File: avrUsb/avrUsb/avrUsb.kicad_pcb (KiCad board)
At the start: 4 copper layers, 53 x 59 mm, 15 parts, among them J1 Screw_Terminal_01x07, J2 Screw_Terminal_01x10, J3 Screw_Terminal_01x10, U1 ATmega8U2-AU, X1 USBFCI_10103594, Y1 8 Mhz

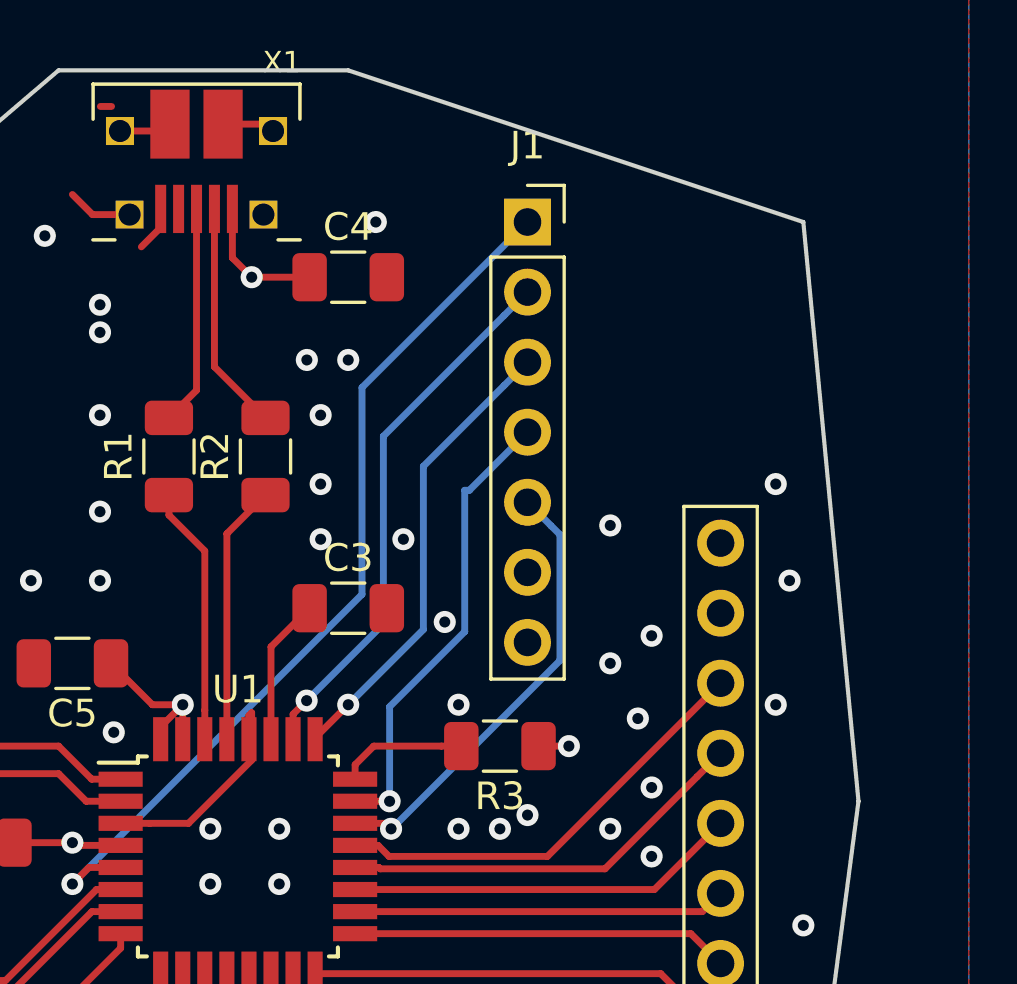
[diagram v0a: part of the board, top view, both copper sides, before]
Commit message: updated usb polarity + reset header
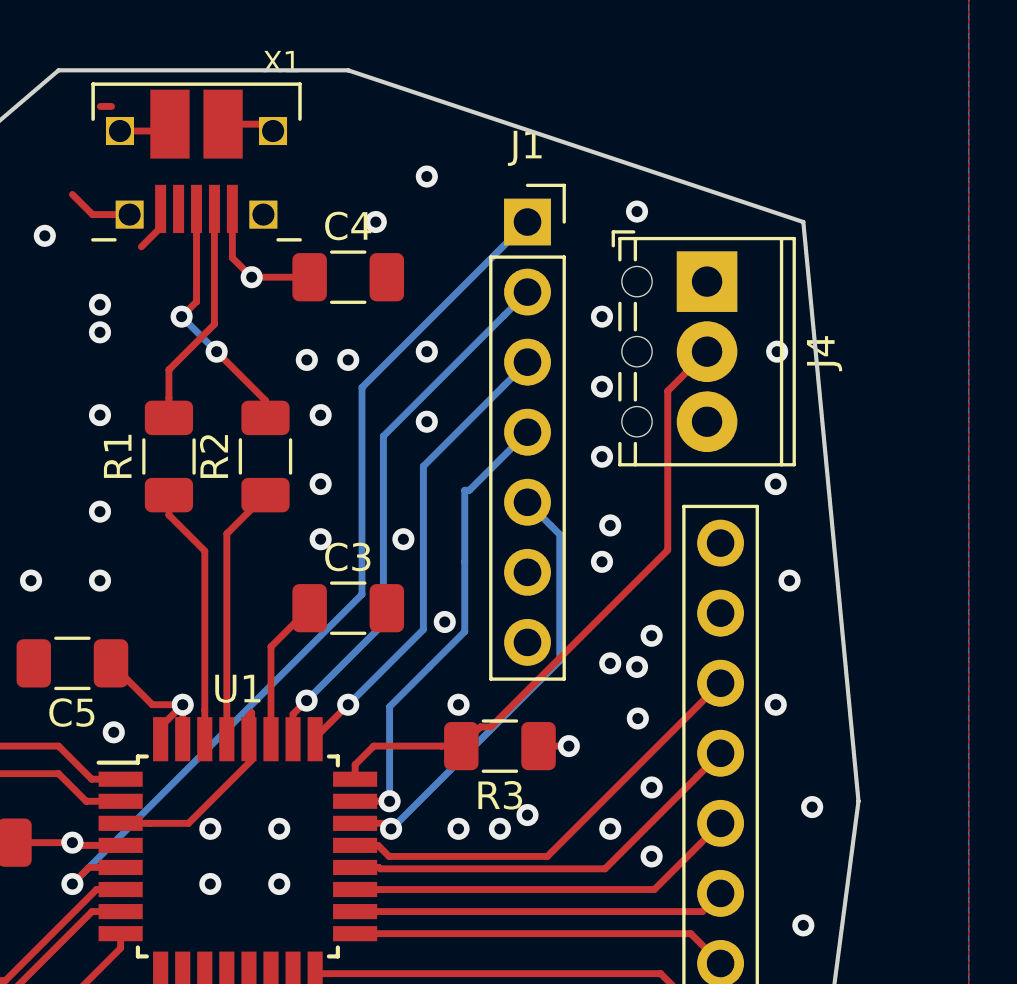
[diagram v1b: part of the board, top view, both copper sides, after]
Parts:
- added J4: Screw_Terminal_01x03, TerminalBlock_Phoenix:TerminalBlock_Phoenix_MPT-0,5-3-2.54_1x03_P2.54mm_Horizontal, F.Cu at (207.0, 73.7)
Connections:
- X1 pad D+: Net-(R1-Pad2) -> Net-(R2-Pad2)
- X1 pad D-: Net-(R2-Pad2) -> Net-(R1-Pad2)
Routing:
- net Net-(J4-Pad2): track 4.65 -> 22.9 mm
- net Net-(R2-Pad2): track 8.34 -> 9.06 mm, vias 0 -> 2
- net GND: track 16.3 -> 16.7 mm, vias 78 -> 89

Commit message: QFN
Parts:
- U1: value ATmega8U2-AU -> ATmega32U2-MU
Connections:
- U1 pad 10: Net-(J3-Pad5) -> Net-(J1-Pad2)
- U1 pad 11: Net-(J3-Pad6) -> Net-(J1-Pad3)
- U1 pad 12: Net-(J3-Pad7) -> Net-(J1-Pad4)
- U1 pad 13: Net-(J3-Pad8) -> Net-(J1-Pad5)
- U1 pad 22: Net-(J1-Pad5) -> Net-(J3-Pad5)
- U1 pad 23: Net-(J1-Pad4) -> Net-(J3-Pad4)
- U1 pad 25: Net-(J1-Pad3) -> Net-(J3-Pad3)
- U1 pad 26: Net-(J1-Pad2) -> Net-(J3-Pad2)
- U1 pad 5: Net-(J1-Pad1) -> Net-(J3-Pad1)
- U1 pad 6: Net-(J3-Pad1) -> Net-(J3-Pad6)
- U1 pad 7: Net-(J3-Pad2) -> Net-(J3-Pad7)
- U1 pad 8: Net-(J3-Pad3) -> Net-(J3-Pad8)
- U1 pad 9: Net-(J3-Pad4) -> Net-(J1-Pad1)
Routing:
- net Net-(J3-Pad3): track 16.4 -> 77.8 mm, vias 0 -> 1
- net Net-(J3-Pad2): track 15.3 -> 66.5 mm, vias 0 -> 1
- net Net-(J3-Pad5): track 20.4 -> 55.2 mm, vias 0 -> 1
- net Net-(J3-Pad4): track 18.3 -> 42.7 mm, vias 0 -> 1
- net Net-(J1-Pad1): track 32.8 -> 53.1 mm
- net Net-(J1-Pad2): track 19.7 -> 36.7 mm
- net Net-(J1-Pad3): track 16.9 -> 33.6 mm
- net Net-(J1-Pad4): track 16.8 -> 31.0 mm
- net Net-(J1-Pad5): track 16.3 -> 29.2 mm
- net Net-(J3-Pad6): track 22.2 -> 24.7 mm
- net Net-(J3-Pad1): track 14.6 -> 16.0 mm
- net Net-(J3-Pad8): track 26.0 -> 27.3 mm
- net Net-(J3-Pad7): track 24.1 -> 25.4 mm
- net GND: vias 89 -> 85
